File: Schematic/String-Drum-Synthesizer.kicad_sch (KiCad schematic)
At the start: 31 parts, among them U1 LM1117MP-3.3, U2 OPA1679, U3 74HC4051, U4 STM32F205RCTx, U5 LM1117MP-3.3

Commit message: Most recent schematic
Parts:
- removed unit 4 of U2
- removed U3: 74HC4051, symbol 74xx:74HC4051
- added C7: 0.01u, symbol Device:C
- added C8: 10u, symbol Device:C
- added J1: USB_B, symbol Connector:USB_B
- added Pot9: Volume (100k), symbol Connector:Conn_01x03_Pin
- added R13, R14: 750, symbol Device:R
- added U3: LM3900, symbol Amplifier_Operational:OPA1679
- added U6: LM3900DR, D14, symbol 2024-10-03_04-50-33:LM3900DR
- R10, R3, R4: value 16 -> 114
- R5: value 10k -> 114
- R6: value 1k -> 75k
- R7, R8: value 33 -> 114
- U2: value OPA1679 -> LM3900
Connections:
- net +2V5: now also R7.2, C7.1, R14.2
- net +3V3: no longer R7.2
- net +5V: now also J1.1 (VBUS)
- net DAC Out: now also C8.1; no longer R6.1
- net GND: now also J1.4 (GND), J1.5 (Shield); no longer R8.1
- net at R3.2, R4.1: now also U3.2 (-)
- net at R10.1: now also U3.3 (+)
- net at R6.2, U2.2 (-): now also Pot9.1 (Pin_1); no longer R5.1
- net at R3.1, U2.1: now also R5.1, Pot9.2 (Pin_2), Pot9.3 (Pin_3); no longer R5.2
- net at R7.1: now also U3.12 (+); no longer R8.2
- net Audio Out renamed Audio Out L
- net Audio Out L: now also U3.1
- new net: C7.2, R13.2, R6.1
- new net: C8.2, R13.1, R14.1
- new net: R5.2, R8.1, U3.13 (-)
- new net Audio Out R: R8.2, U3.14
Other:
- moved on the sheet: R10, R3, R4, R6, R9, U2A, U4

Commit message: Updated Amplifier Resistor Values
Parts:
- R10, R3, R5, R7, R8: value 114 -> 110
- R14: value 750 -> 820
- R9: value 1k -> 75k
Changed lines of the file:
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@@
 			)
 		)
-		(property "Value" "114"
+		(property "Value" "110"
 			(at -82.55 19.0499 0)
 			(effects
@@
 			)
 		)
-		(property "Value" "114"
+		(property "Value" "110"
 			(at -87.63 -10.16 90)
 			(effects
@@
 			)
 		)
-		(property "Value" "750"
+		(property "Value" "820"
 			(at -154.94 -7.6201 0)
 			(effects
@@
 			)
 		)
-		(property "Value" "114"
+		(property "Value" "110"
 			(at -82.55 -15.2401 0)
 			(effects
@@
 			)
 		)
-		(property "Value" "114"
+		(property "Value" "110"
 			(at -87.63 22.86 90)
 			(effects
@@
 			)
 		)
-		(property "Value" "1k"
+		(property "Value" "75k"
 			(at -118.11 -12.7001 0)
 			(effects
@@
 			)
 		)
-		(property "Value" "114"
+		(property "Value" "110"
 			(at -69.85 35.56 90)
 			(effects

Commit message: Final Schematic For Demo
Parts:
- removed U4: STM32F205RCTx, Package_QFP:LQFP-64_10x10mm_P0.5mm, symbol MCU_ST_STM32F2:STM32F205RCTx
- removed U6: LM3900DR, D14, symbol 2024-10-03_04-50-33:LM3900DR
- added C9: 2.2uF, symbol Device:C
- added J2: USB_A, symbol Connector:USB_A
- added R15: 10k, symbol Device:R
- added U6: STM32F722RCTx, Package_QFP:LQFP-64_10x10mm_P0.5mm, symbol MCU_ST_STM32F7:STM32F722RCTx
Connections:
- net +3V3: now also U6.1 (VBAT), U6.13 (VDDA), U6.19 (VDD), U6.32 (VDD), U6.48 (VDD), U6.64 (VDD)
- net +5V: now also J2.1 (VBUS)
- net DAC Out: now also U6.20 (PA4)
- net GND: now also C9.2, J2.4 (GND), J2.5 (Shield), R15.1, U6.12 (VSSA), U6.18 (VSS), U6.31 (VSS), U6.47 (VSS), U6.63 (VSS), U6.7 (NRST)
- net USB_DM: now reaches J1.2 (D-)
- net USB_DM: now also U6.44 (PA11)
- net USB_DP: now reaches J1.3 (D+)
- net USB_DP: now also U6.45 (PA12)
- net EmotiveKnobValue6: now reaches Pot6.2 (Pin_2)
- net EmotiveKnobValue6: now also U6.25 (PB0)
- net EmotiveKnobValue0: now reaches Pot0.2 (Pin_2)
- net EmotiveKnobValue0: now also U6.14 (PA0)
- net EmotiveKnobValue7: now reaches Pot7.2 (Pin_2)
- net EmotiveKnobValue7: now also U6.26 (PB1)
- net EmotiveKnobValue4: now reaches Pot4.2 (Pin_2)
- net EmotiveKnobValue4: now also U6.22 (PA6)
- net EmotiveKnobValue5: now reaches Pot5.2 (Pin_2)
- net EmotiveKnobValue5: now also U6.23 (PA7)
- net EmotiveKnobValue1: now reaches Pot1.2 (Pin_2)
- net EmotiveKnobValue1: now also U6.15 (PA1)
- net EmotiveKnobValue3: now reaches Pot3.2 (Pin_2)
- net EmotiveKnobValue3: now also U6.17 (PA3)
- net EmotiveKnobValue2: now reaches Pot2.2 (Pin_2)
- net EmotiveKnobValue2: now also U6.16 (PA2)
- new net: C9.1, U6.30 (VCAP_1)
- new net: U6.5 (PH0), U6.6 (PH1)
- new net: R15.2, U6.60 (BOOT0)
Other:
- moved on the sheet: C7, C8, J1, Pot0, Pot1, Pot2, Pot3, Pot4, Pot5, Pot6, Pot7, Pot9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

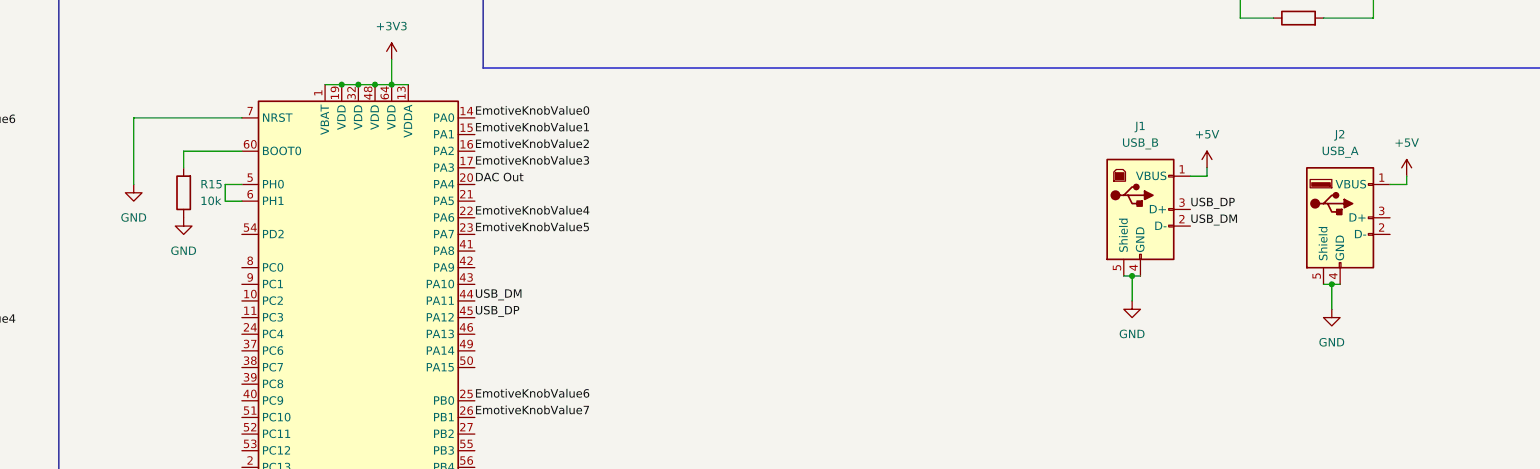
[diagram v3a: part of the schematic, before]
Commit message: Deleted a USB Port
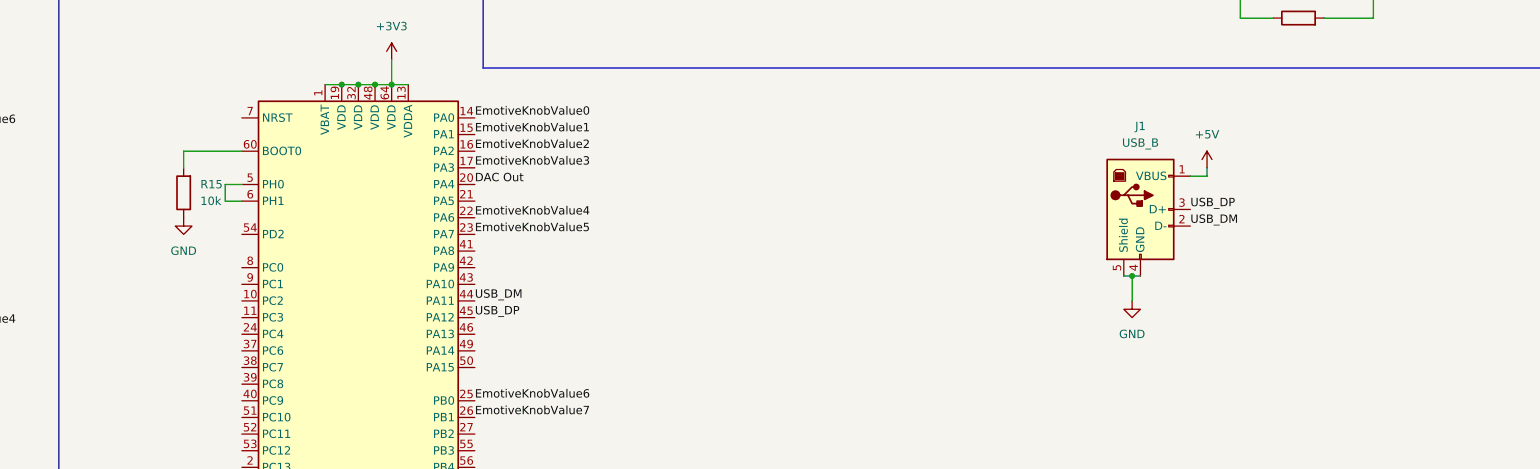
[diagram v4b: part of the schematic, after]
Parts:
- removed J2: USB_A, symbol Connector:USB_A
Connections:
- net GND: no longer U6.7 (NRST)

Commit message: Port added to schematic, but needs connections
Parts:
- added C10, C11: 400pF, symbol Device:C
- added J2: USB_A, symbol Connector:USB_A
- added J3: HDMI_A_1.4, symbol Connector:HDMI_A_1.4
- R4: value 114 -> 110
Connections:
- net +5V: now also J2.1 (VBUS), J3.18 (+5V)
- net Audio Out L: now also C11.2
- net Audio Out R: now also C10.2
- net GND: now also J2.4 (GND), J2.5 (Shield), J3.17 (GND)
- net at R3.2, R4.1, U3.2 (-): now also C11.1
- net at R5.2, R8.1, U3.13 (-): now also C10.1
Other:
- moved on the sheet: C1, C2, C3, C4, C5, C6, C7, C8, C9, J1, Pot0, Pot1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

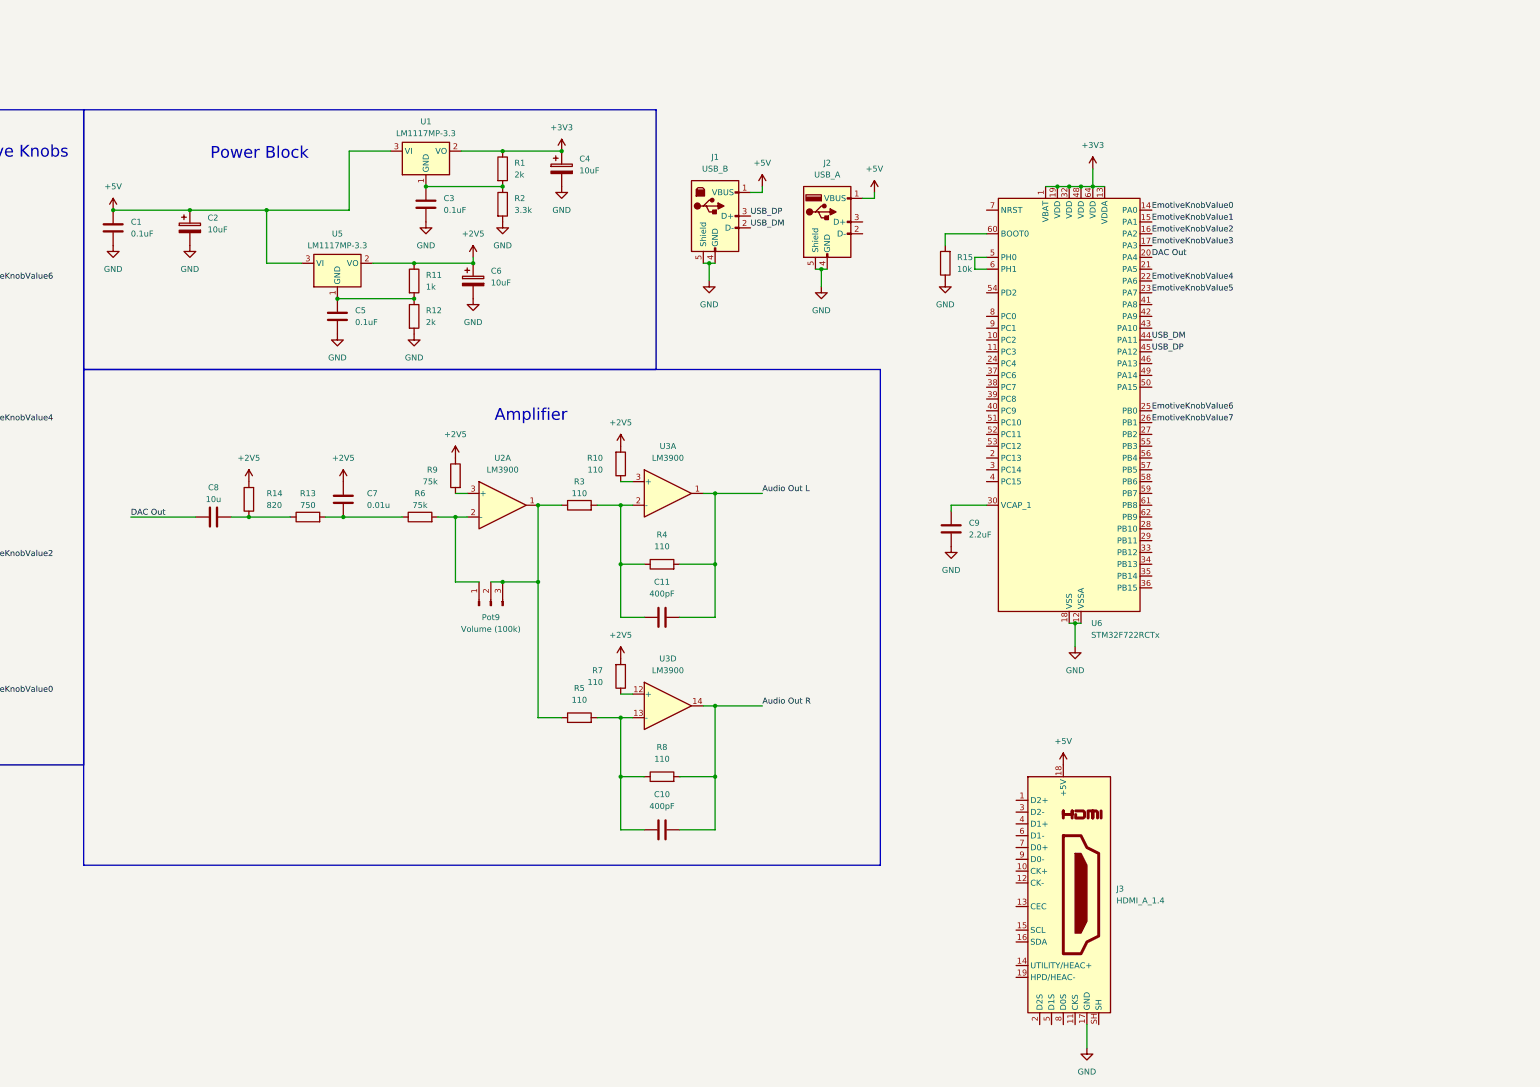
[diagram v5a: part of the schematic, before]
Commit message: Switched out op-amp for actual LM3900
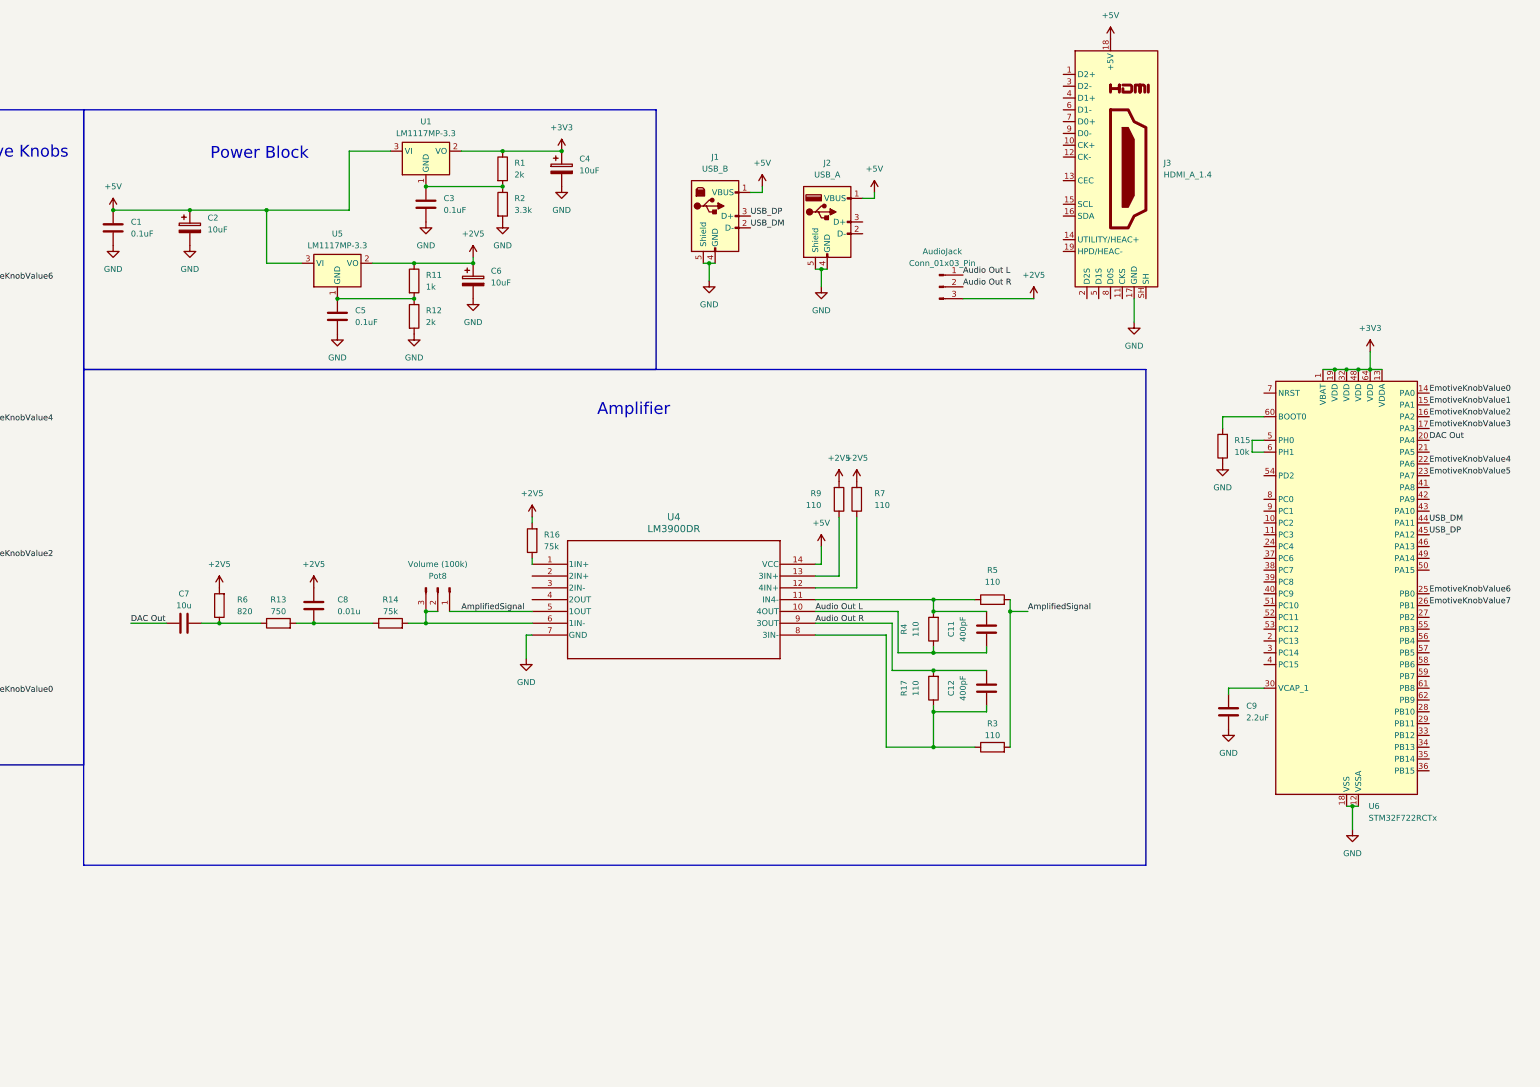
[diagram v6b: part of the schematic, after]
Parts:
- removed C10: 400pF, symbol Device:C
- removed Pot9: Volume (100k), symbol Connector:Conn_01x03_Pin
- removed R10, R8: 110, symbol Device:R
- removed U2, U3: LM3900, symbol Amplifier_Operational:OPA1679
- added AudioJack: Conn_01x03_Pin, symbol Connector:Conn_01x03_Pin
- added C12: 400pF, symbol Device:C
- added Pot8: Volume (100k), symbol Connector:Conn_01x03_Pin
- added R16: 75k, symbol Device:R
- added R17: 110, symbol Device:R
- added U4: LM3900DR, D14, symbol 2024-10-03_04-50-33:LM3900DR
- C7: value 0.01u -> 10u
- C8: value 10u -> 0.01u
- R14: value 820 -> 75k
- R6: value 75k -> 820
- R9: value 75k -> 110
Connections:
- net +2V5: now also C8.1, R6.2, R9.2, AudioJack.3 (Pin_3), R16.2; no longer C7.1, R14.2, R9.1
- net +5V: now also U4.14 (VCC)
- net Audio Out L: now also C11.1, R4.1, AudioJack.1 (Pin_1), U4.10 (4OUT); no longer C11.2, R4.2
- net Audio Out R: now also AudioJack.2 (Pin_2), C12.2, R17.2, U4.9 (3OUT)
- net DAC Out: now also C7.1; no longer C8.1
- net GND: now also U4.7 (GND)
- net at C7.2, R6.1: now also R13.1; no longer R13.2
- net at C8.2, R14.1: now also R13.2; no longer R13.1
- net at R5.1: now also C11.2, R4.2, U4.11 (IN4-); no longer R3.1
- net at R7.1: now also U4.12 (4IN+)
- net AmplifiedSignal: now reaches R5.2
- net AmplifiedSignal: now also R3.2, Pot8.1 (Pin_1), U4.5 (1OUT)
- new net: R16.1, U4.1 (1IN+)
- new net: R9.1, U4.13 (3IN+)
- new net: Pot8.2 (Pin_2), Pot8.3 (Pin_3), R14.2, U4.6 (1IN-)
- new net: C12.1, R17.1, R3.1, U4.8 (3IN-)
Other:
- moved on the sheet: C9, J3, R15, U6
